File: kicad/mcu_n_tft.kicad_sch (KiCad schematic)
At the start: 19 parts, among them J301 Conn_01x05, J303 Conn_ARM_SWD_TagConnect_TC2030, J304 TSM-105-01-L-DH, U301 BL654, Y301 Crystal

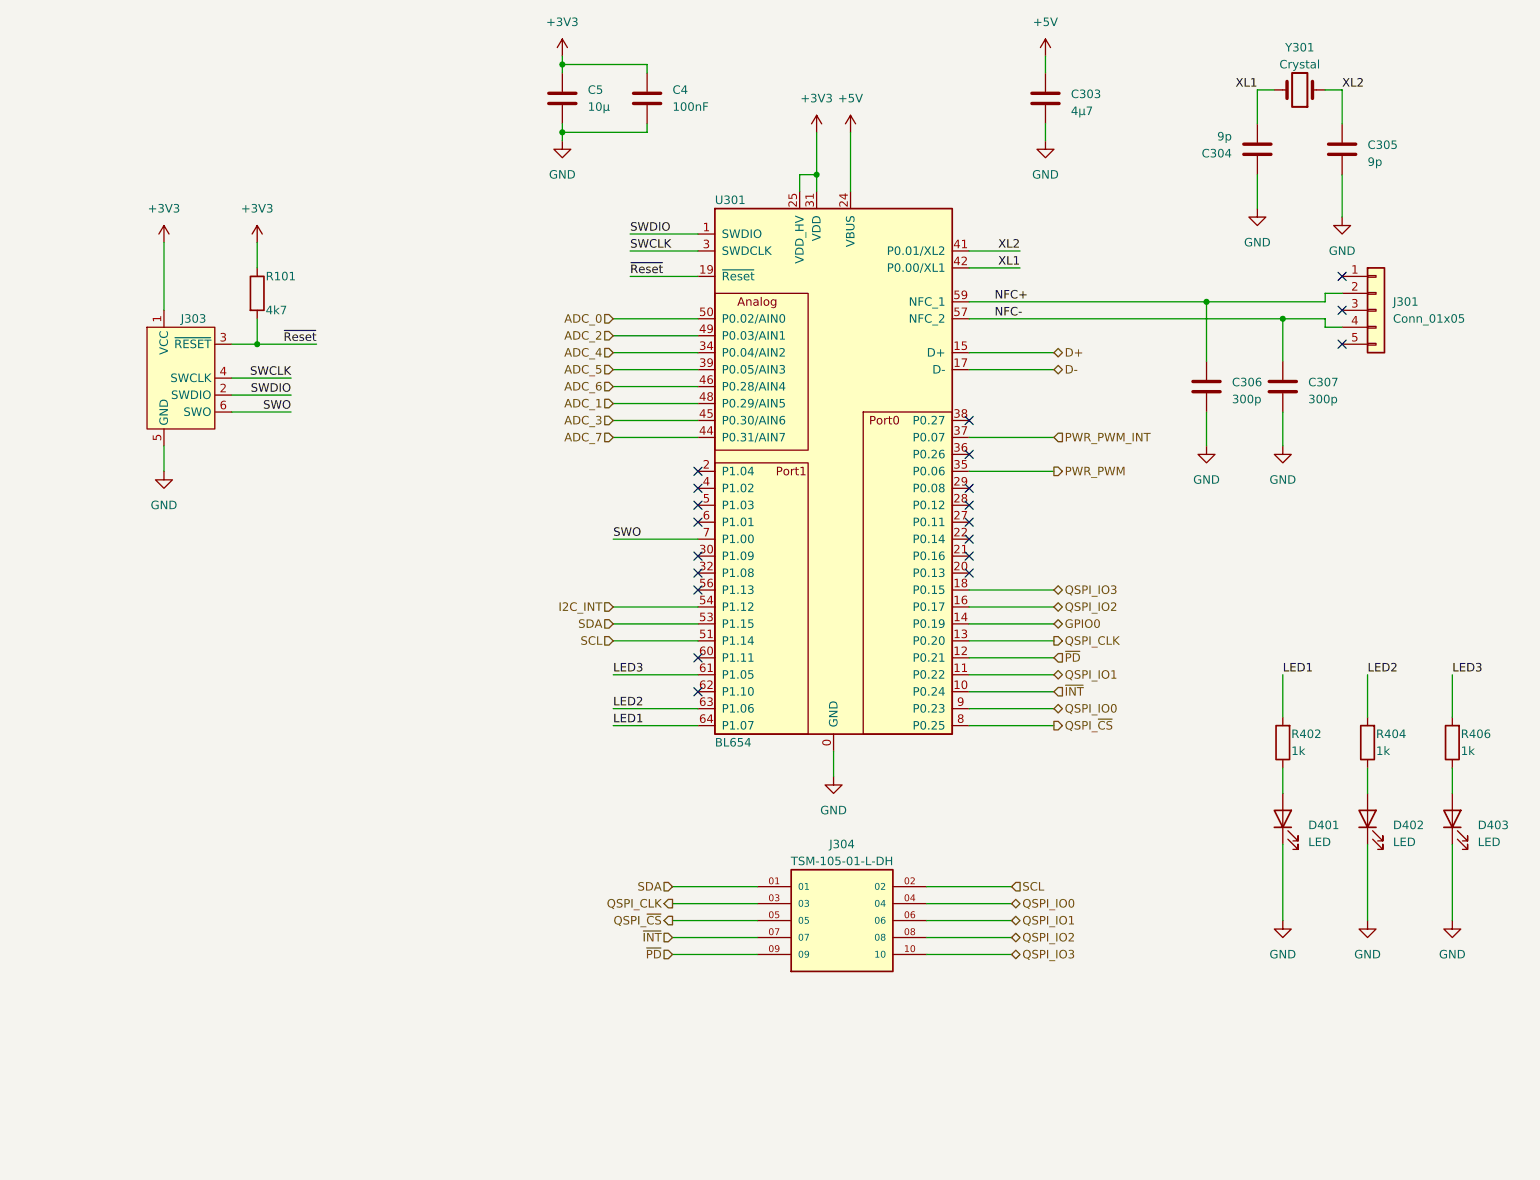
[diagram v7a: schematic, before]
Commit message: rework board
add nrf 7002
add oled display
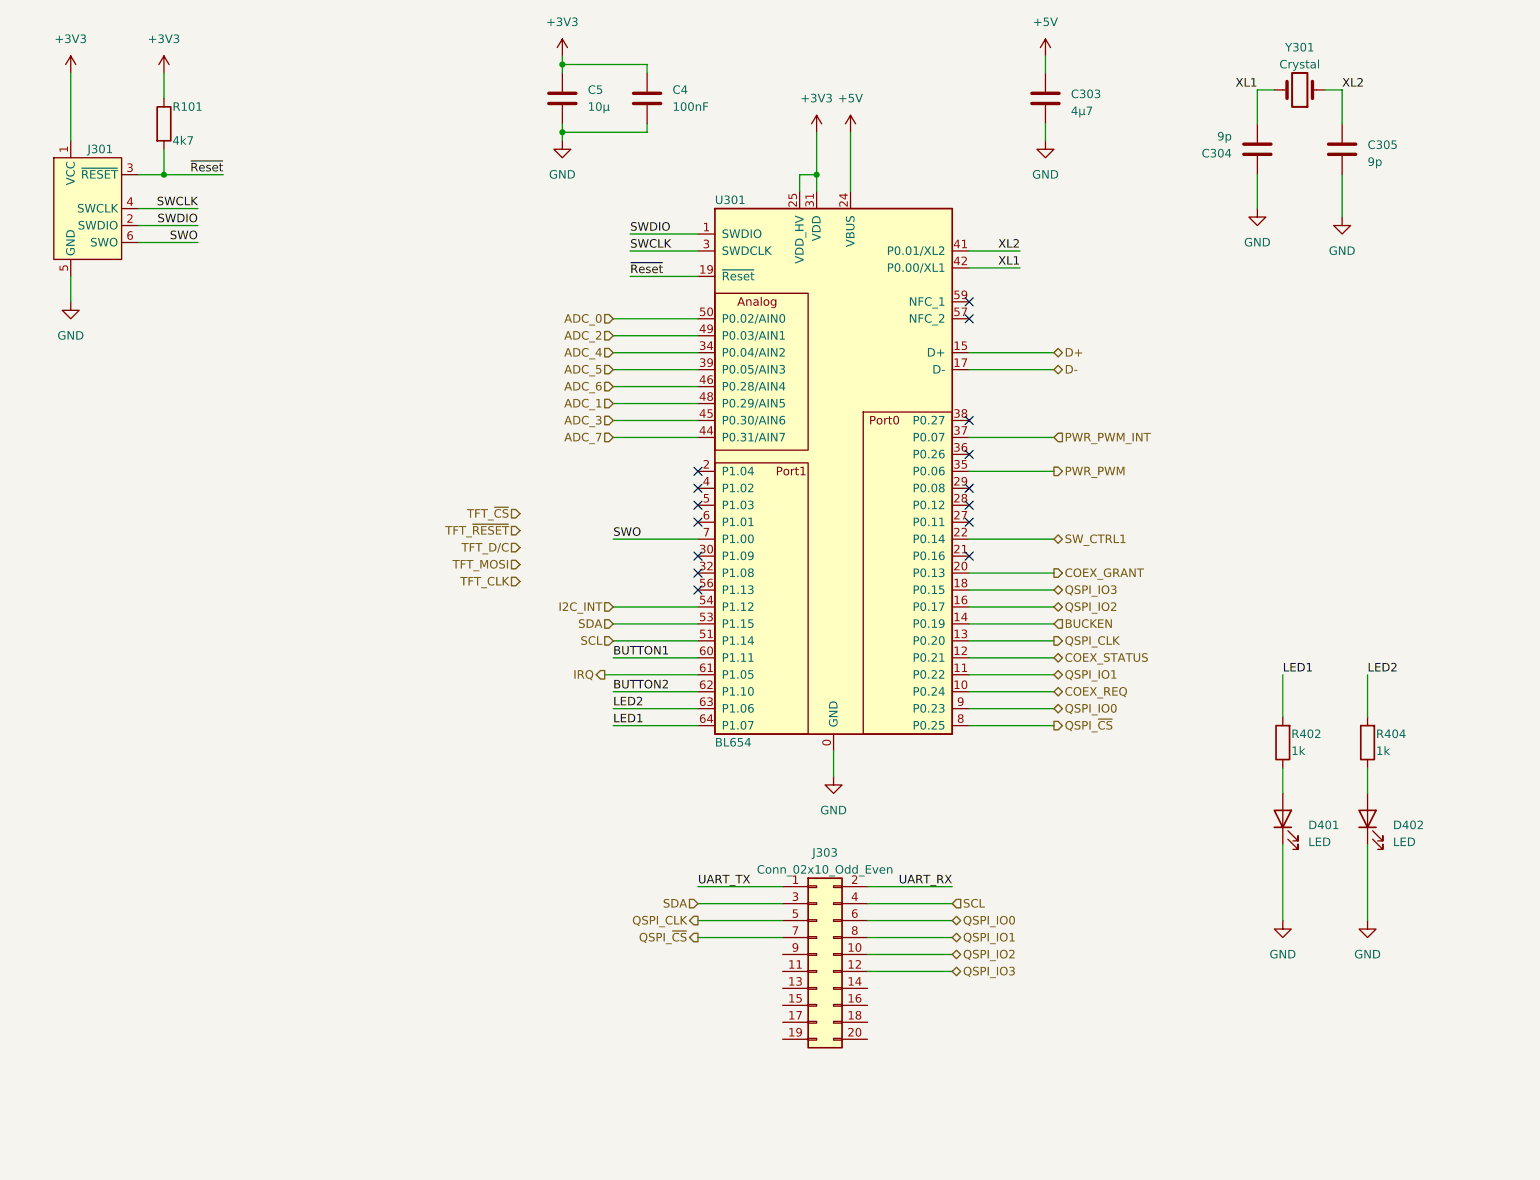
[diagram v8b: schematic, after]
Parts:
- removed C306, C307: 300p, Capacitor_SMD:C_0603_1608Metric, symbol Device:C
- removed D403: LED, LED_SMD:LED_0603_1608Metric, symbol Device:LED
- removed J301: Conn_01x05, mylib_connector:Easy-On 51281-5, symbol Connector_Generic:Conn_01x05
- removed J304: TSM-105-01-L-DH, mylib_connector:SAMTEC_TSM-105-01-L-DH, symbol mylib_connectors:TSM-105-01-L-DH
- removed R406: 1k, Resistor_SMD:R_0603_1608Metric, symbol Device:R
- added J303: Conn_02x10_Odd_Even, Connector_PinHeader_1.27mm:PinHeader_2x10_P1.27mm_Vertical_SMD, symbol Connector_Generic:Conn_02x10_Odd_Even
- renumbered J303 to J301
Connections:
- net QSPI_CLK: now also J303.5 (Pin_5)
- net QSPI_IO0: now also J303.6 (Pin_6)
- net QSPI_IO1: now also J303.8 (Pin_8)
- net QSPI_IO2: now also J303.10 (Pin_10)
- net QSPI_IO3: now also J303.12 (Pin_12)
- net QSPI_~{CS}: now also J303.7 (Pin_7)
- net SCL: now also J303.4 (Pin_4)
- net SDA: now also J303.3 (Pin_3)
- net COEX_GRANT: now reaches U301.20 (P0.13)
- net SW_CTRL1: now reaches U301.22 (P0.14)
- net BUTTON1: now reaches U301.60 (P1.11)
- net BUTTON2: now reaches U301.62 (P1.10)
- net GPIO0 renamed BUCKEN
- net LED3 renamed IRQ
- net NFC+: no longer names the net of U301.59 (NFC_1)
- net NFC-: no longer names the net of U301.57 (NFC_2)
- net ~{INT} renamed COEX_REQ
- net ~{PD} renamed COEX_STATUS
- new net UART_RX: J303.2 (Pin_2)
- new net UART_TX: J303.1 (Pin_1)
- no-connect marks 20 -> 15
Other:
- title: (none) -> Firewaterburn
- moved on the sheet: J301, R101
